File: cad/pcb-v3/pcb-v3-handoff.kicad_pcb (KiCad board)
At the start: 4 copper layers, 19.3 x 19.3 mm, 46 parts

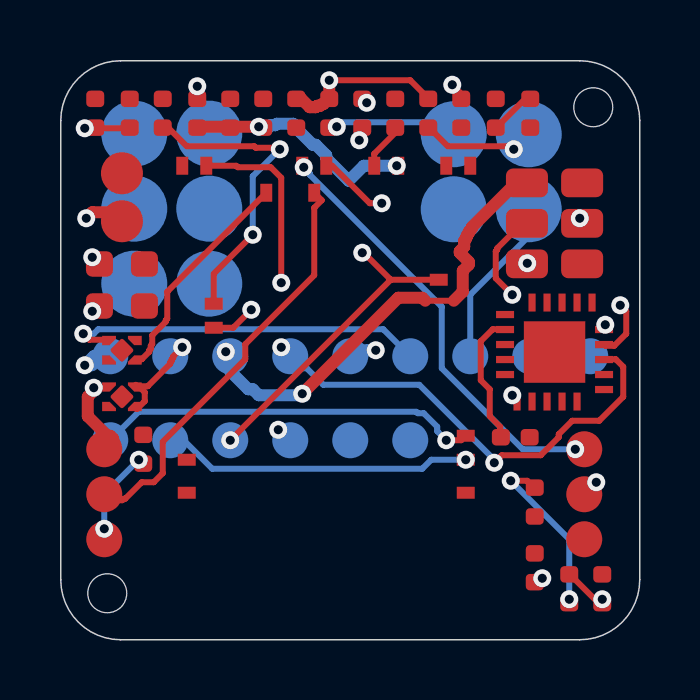
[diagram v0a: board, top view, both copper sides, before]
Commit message: pcb-v3: per-net plane-clean routing -> 12 opens with intact plane, 0 DRC, min track 0.200. Left column proven over-packed (0.225mm max gap vs 0.60 needed); BT1 is the cap. Board is over-subscribed in three places.
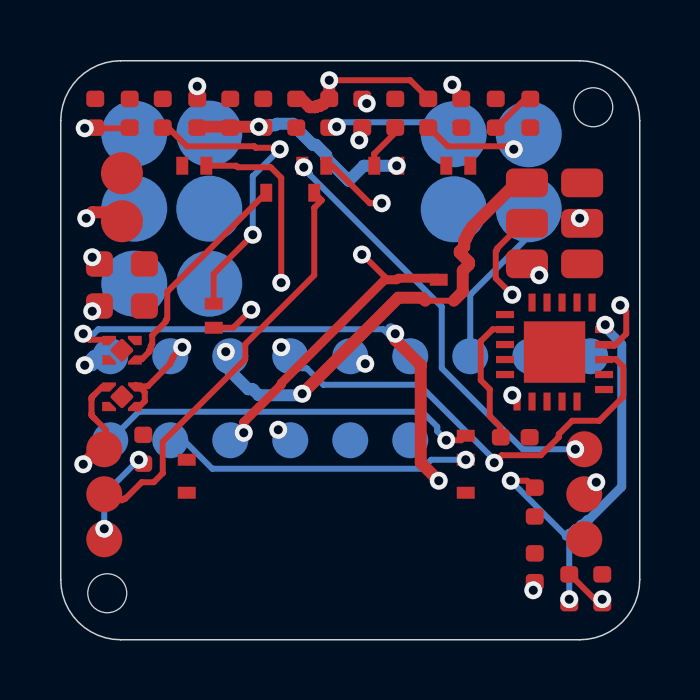
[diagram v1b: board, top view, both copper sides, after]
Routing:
- net SENSOR_MCU_3V3: track 15.5 -> 32.6 mm, vias 3 -> 5
- net OK_HYST: track 5.77 -> 13.8 mm
- net SENSOR_3V3: track 30.7 -> 34.0 mm
- net VBAT_OK: track 28.0 -> 30.2 mm

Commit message: pcb-v3: C1/C2 0603->0402 into the packer, C5/C7 0805->0603, left column down to U3+U4. 22 parts in 22 slots. Route: 12 -> 7 opens, plane untouched naturally, min track 0.200, vias 0.6/0.3.
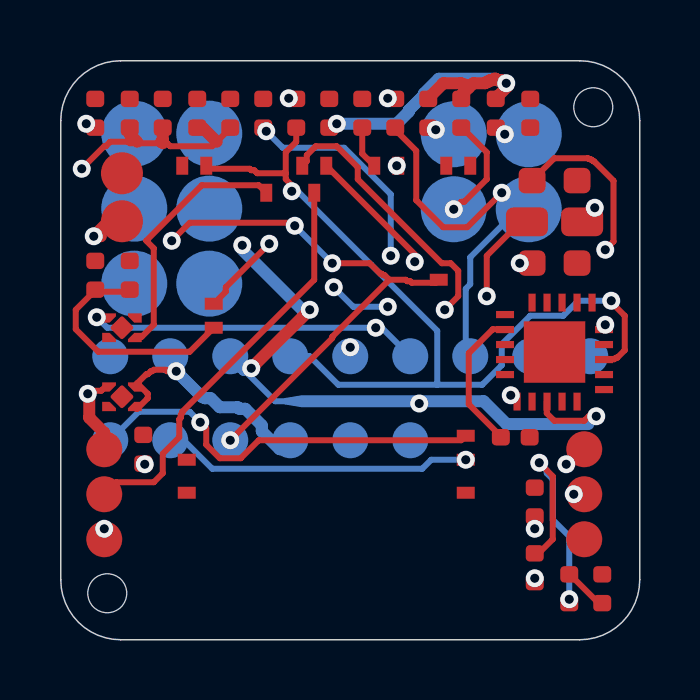
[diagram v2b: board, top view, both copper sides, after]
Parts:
- moved C6 17.6 mm to (-2.90, -7.90)
- moved ROV2 13.0 mm to (6.15, 5.06)
- moved C1 9.44 mm to (-0.70, -7.90), turned to 90 degrees
- moved C2 5.62 mm to (-5.10, -7.90), turned to 90 degrees
- moved C12 5.52 mm to (-8.50, -2.50)
- moved R5 5.52 mm to (-7.35, -2.50)
- moved R3 5.50 mm to (3.70, -7.90)
- moved R1 3.30 mm to (2.60, -7.90)
- moved C10 2.25 mm to (-6.25, -7.90)
- moved C13 2.25 mm to (-8.50, -7.90)
- moved R4 2.25 mm to (-7.35, -7.90)
- moved R2 2.25 mm to (4.85, -7.90)
- moved R6 2.20 mm to (1.50, -7.90)
- moved R7 2.20 mm to (-1.80, -7.90)
- moved ROK3 2.19 mm to (6.15, 7.25)
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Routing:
- net VBAT: track 23.5 -> 53.0 mm, vias 3 -> 9
- net VSTOR: track 16.1 -> 39.1 mm, vias 5 -> 3
- net OK_PROG: track 13.6 -> 1.55 mm, vias 2 -> 0
- net RESET: track 16.2 -> 24.4 mm, vias 3 -> 5
- net SENSOR_MCU_3V3: track 32.6 -> 24.6 mm, vias 5 -> 4
- net VBAT_SENSE: track 15.9 -> 8.04 mm, vias 3 -> 0
- net BL_RETURN: track 5.71 -> 13.2 mm, vias 0 -> 1
- net VIN_DC: track 9.81 -> 17.1 mm, vias 4 -> 3
- net SENSOR_3V3: track 34.0 -> 28.4 mm, vias 4 -> 5
- net SENSOR_TX: track 14.5 -> 18.2 mm
- net HARV_3: track 0.00 -> 3.60 mm, vias 0 -> 1
- net HARV_1: track 4.40 -> 0.86 mm
- net HARV_2: track 3.85 -> 1.18 mm
- net VRDIV: track 0.00 -> 2.36 mm, vias 0 -> 2
- net BL_FLAG: track 17.5 -> 19.8 mm
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
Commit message: pcb-v3: silkscreen (F.Fab designators, pin-1 dots, back identity block). Fix two checker bugs: KiCad Y-down rotation sign (79 phantom shorts) and rule-area layer scoping (47 phantom boxed pads). All gates clean; 7 opens, plane intact.
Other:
- board text added: "BT1 +"
- board text added: "Daniel Rivera"
- board text added: "J2"
- board text added: "TouchID v3 2026"
- board text added: "U1"
- board text added: "U2"
- board text added: "driver0"

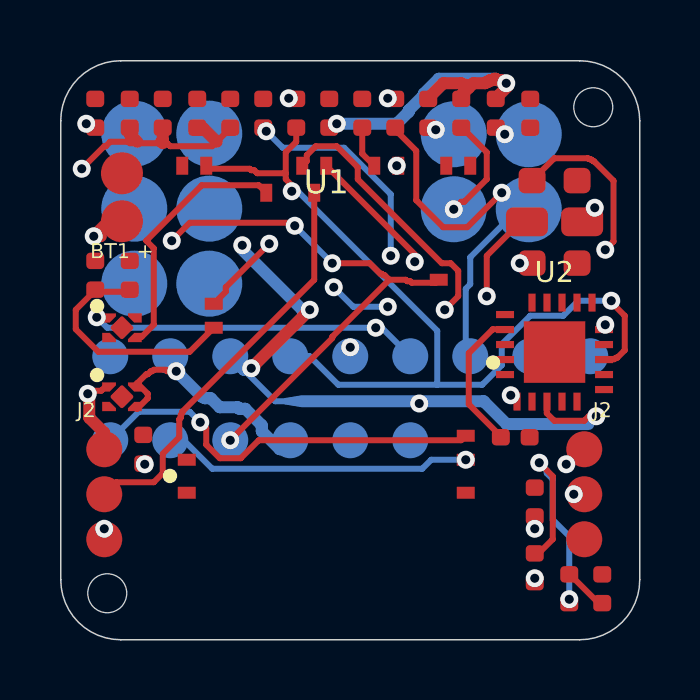
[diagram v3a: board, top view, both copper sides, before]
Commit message: pcb-v3: emit Raytac's second (top-layer-only) antenna keep-out. It was captured in mdbt50q_footprint.py as KEEPOUT_TOP and never written to the board.
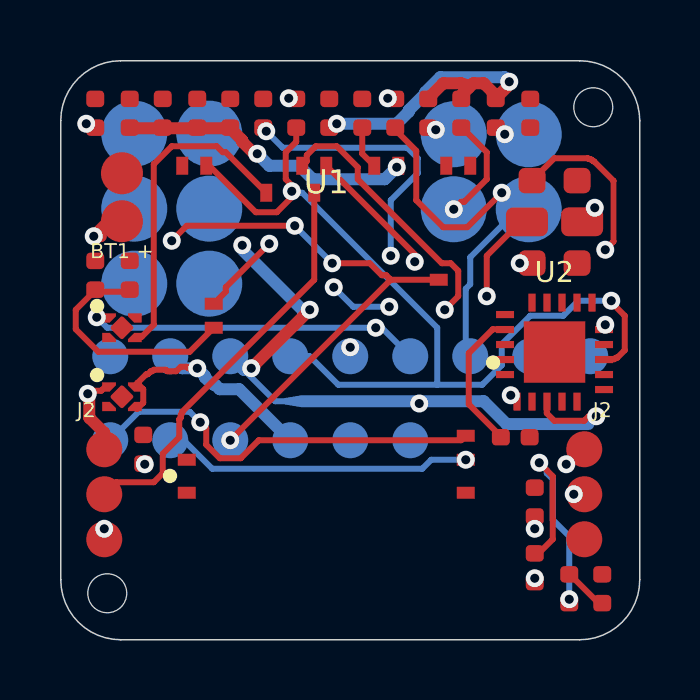
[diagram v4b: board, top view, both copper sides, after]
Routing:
- net VSTOR: track 39.1 -> 28.1 mm
- net SENSOR_SW_EN: track 8.44 -> 10.7 mm
- net SENSOR_3V3: track 28.4 -> 30.4 mm
- net VBAT_OK: track 28.9 -> 30.1 mm

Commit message: pcb-v3: re-source footprints from JLCPCB (L1 0.96->2.20mm was badly wrong), keep TI's land for U2 where JLC's is wider and riskier. Remove name from silk, add connector pinout labels + pin-1 dots.
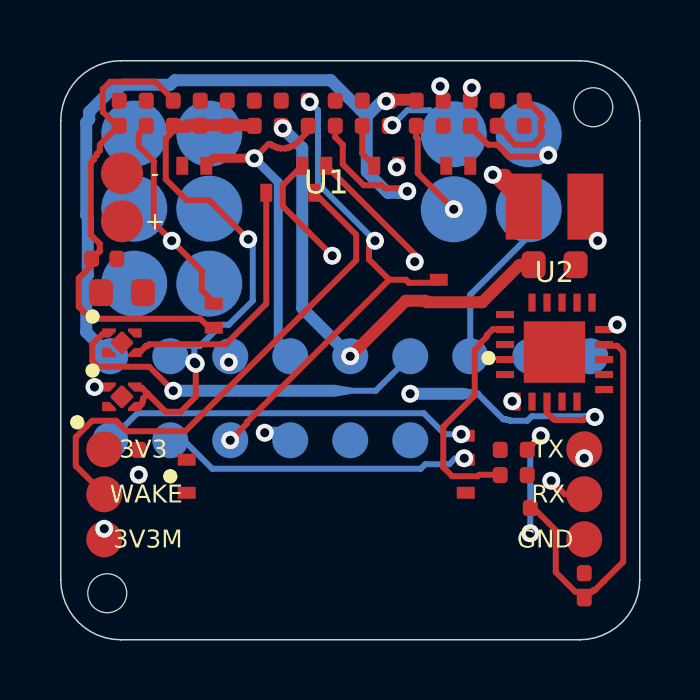
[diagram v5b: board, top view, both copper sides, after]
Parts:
- moved C5 14.9 mm to (-7.61, -1.92)
- moved ROV2 13.0 mm to (5.80, -7.90)
- moved R5 5.41 mm to (-7.70, -7.90)
- moved ROK3 3.52 mm to (5.90, 3.74)
- moved ROK2 2.62 mm to (6.00, 5.68)
- moved C2 1.90 mm to (-3.20, -7.90)
- moved C13 1.70 mm to (-6.80, -7.90)
- moved R6 1.60 mm to (3.10, -7.90)
- moved R3 1.50 mm to (2.20, -7.90)
- moved R4 1.45 mm to (-5.90, -7.90)
- moved R1 1.30 mm to (1.30, -7.90)
- moved C10 1.25 mm to (-5.00, -7.90)
- moved ROV1 1.10 mm to (4.90, -7.90)
- moved C4 0.98 mm to (5.00, 3.74), turned to 90 degrees
- moved R2 0.85 mm to (4.00, -7.90)
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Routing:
- net VBAT: track 53.0 -> 15.7 mm, vias 9 -> 3
- net VIN_DC: track 17.0 -> 36.5 mm, vias 3 -> 4
- net VBAT_OK: track 30.1 -> 11.3 mm, vias 2 -> 1
- net OK_PROG: track 1.55 -> 13.2 mm
- net RESET: track 24.4 -> 16.2 mm, vias 5 -> 3
- net VBAT_SENSE: track 8.04 -> 15.9 mm
- net BL_RETURN: track 13.2 -> 5.71 mm, vias 1 -> 0
- net SENSOR_MCU_3V3: track 24.6 -> 18.5 mm, vias 4 -> 3
- net OK_HYST: track 14.1 -> 9.53 mm
- net SENSOR_3V3: track 30.4 -> 26.5 mm, vias 5 -> 3
- net SENSOR_WAKEUP: track 13.7 -> 17.2 mm
- net VBAT_OV_SET: track 0.00 -> 3.46 mm
- net VREF_SAMP: track 4.77 -> 7.73 mm
- net HARV_2: track 1.18 -> 3.97 mm
- net VRDIV: track 2.36 -> 0.00 mm, vias 2 -> 0
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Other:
- board text added: "+"
- board text added: "-"
- board text added: "3V3"
- board text added: "3V3M"
- board text added: "CLK"
- board text added: "DIO"
- board text added: "GND"
- board text added: "RST"
- board text added: "RX"
- board text added: "TX"
- board text added: "VDD"
- board text added: "WAKE"
- board text removed: "BT1 +"
- board text removed: "Daniel Rivera"
- board text removed: "J2"

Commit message: 3D: generate STEP bodies at verified dimensions and attach to all 29 footprints so KiCad Alt+3 shows real geometry. Re-route: 8 opens, plane intact.
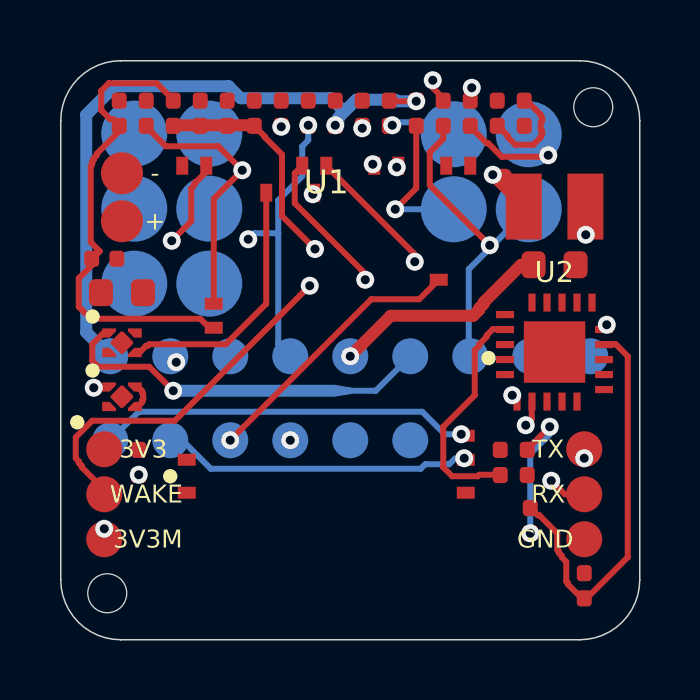
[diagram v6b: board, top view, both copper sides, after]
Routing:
- net VBAT: track 15.7 -> 0.00 mm, vias 3 -> 0
- net VSTOR: track 30.4 -> 39.1 mm
- net RESET: track 16.2 -> 9.17 mm, vias 3 -> 1
- net VIN_DC: track 36.5 -> 29.9 mm
- net BL_RETURN: track 5.71 -> 10.8 mm, vias 0 -> 1
- net VBAT_OK: track 11.3 -> 15.2 mm, vias 1 -> 3
- net SENSOR_3V3: track 26.5 -> 24.3 mm
- net HARV_3: track 3.32 -> 5.04 mm
- net SENSOR_WAKEUP: track 17.2 -> 15.6 mm, vias 0 -> 2
- net BL_FLAG: track 18.9 -> 17.7 mm
- net SENSOR_TX: track 17.6 -> 18.5 mm
- net NRF_VDD: track 1.49 -> 1.34 mm, vias 0 -> 2

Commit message: preflight.py: single pre-order gate (15 checks). Found 3 checker bugs of my own (pad-net regex scope, layer-blind keep-outs, silk-vs-wrong-side pads) and 2 real issues (silk over pads, LX has no 0.40 trunk). 13/15 pass.
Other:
- board text removed: "U1"
- board text removed: "U2"
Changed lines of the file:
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@@
-	)
-	(gr_text
-		"U1"
-		(at -0.8 -5.6)
-		(layer "F.SilkS")
-		(effects (font (size 0.8 0.8) (thickness 0.1)))
-	)
-	(gr_text
-		"U2"
-		(at 6.8 -2.6)
-		(layer "F.SilkS")
-		(effects (font (size 0.7 0.7) (thickness 0.1)))
 	)
 	(gr_text
 		"3V3"
-		(at -6.9 3.3)
-		(layer "F.SilkS")
-		(effects (font (size 0.6 0.6) (thickness 0.1)))
-	)
-	(gr_text
-		"3V3"
-		(at -6.9 3.3)
+		(at -6.888 3.3)
 		(layer "F.Fab")
 		(effects (font (size 0.4 0.4) (thickness 0.06)))
@@
 	(gr_text
 		"WAKE"
-		(at -6.8 4.8)
-		(layer "F.SilkS")
-		(effects (font (size 0.6 0.6) (thickness 0.1)))
-	)
-	(gr_text
-		"WAKE"
-		(at -6.8 4.8)
+		(at -6.7 4.8)
 		(layer "F.Fab")
 		(effects (font (size 0.4 0.4) (thickness 0.06)))
@@
 	(gr_text
 		"3V3M"
-		(at -6.75 6.3)
-		(layer "F.SilkS")
-		(effects (font (size 0.6 0.6) (thickness 0.1)))
-	)
-	(gr_text
-		"3V3M"
-		(at -6.75 6.3)
+		(at -6.7 6.3)
 		(layer "F.Fab")
 		(effects (font (size 0.4 0.4) (thickness 0.06)))
@@
 	(gr_text
 		"TX"
-		(at 6.6 3.3)
-		(layer "F.SilkS")
-		(effects (font (size 0.6 0.6) (thickness 0.1)))
-	)
-	(gr_text
-		"TX"
-		(at 6.6 3.3)
+		(at 6.675 3.3)
 		(layer "F.Fab")
 		(effects (font (size 0.4 0.4) (thickness 0.06)))
@@
 	(gr_text
 		"RX"
-		(at 6.6 4.8)
-		(layer "F.SilkS")
-		(effects (font (size 0.6 0.6) (thickness 0.1)))
-	)
-	(gr_text
-		"RX"
-		(at 6.6 4.8)
+		(at 6.675 4.8)
 		(layer "F.Fab")
 		(effects (font (size 0.4 0.4) (thickness 0.06)))
@@
 	(gr_text
 		"GND"
-		(at 6.5 6.3)
-		(layer "F.SilkS")
-		(effects (font (size 0.6 0.6) (thickness 0.1)))
-	)
-	(gr_text
-		"GND"
-		(at 6.5 6.3)
+		(at 6.488 6.3)
 		(layer "F.Fab")
 		(effects (font (size 0.4 0.4) (thickness 0.06)))
@@
 	(gr_text
 		"DIO"
-		(at -8.0 1.9)
-		(layer "B.SilkS")
-		(effects (font (size 0.6 0.6) (thickness 0.1)) (justify mirror))
-	)
-	(gr_text
-		"DIO"
-		(at -8.0 1.9)
+		(at -8.0 2.0)
 		(layer "F.Fab")
 		(effects (font (size 0.4 0.4) (thickness 0.06)))
@@
 	(gr_text
 		"CLK"
-		(at -6.0 1.9)
-		(layer "B.SilkS")
-		(effects (font (size 0.6 0.6) (thickness 0.1)) (justify mirror))
-	)
-	(gr_text
-		"CLK"
-		(at -6.0 1.9)
+		(at -6.0 2.0)
 		(layer "F.Fab")
 		(effects (font (size 0.4 0.4) (thickness 0.06)))
@@
 	(gr_text
 		"RST"
-		(at -4.0 1.9)
-		(layer "B.SilkS")
-		(effects (font (size 0.6 0.6) (thickness 0.1)) (justify mirror))
-	)
-	(gr_text
-		"RST"
-		(at -4.0 1.9)
+		(at -4.0 2.0)
 		(layer "F.Fab")
 		(effects (font (size 0.4 0.4) (thickness 0.06)))
@@
 	(gr_text
 		"VDD"
-		(at -2.0 1.9)
-		(layer "B.SilkS")
-		(effects (font (size 0.6 0.6) (thickness 0.1)) (justify mirror))
-	)
-	(gr_text
-		"VDD"
-		(at -2.0 1.9)
+		(at -2.0 2.0)
 		(layer "F.Fab")
 		(effects (font (size 0.4 0.4) (thickness 0.06)))
@@
 	(gr_text
 		"GND"
-		(at 0.0 1.9)
-		(layer "B.SilkS")
-		(effects (font (size 0.6 0.6) (thickness 0.1)) (justify mirror))
-	)
-	(gr_text
-		"GND"
-		(at 0.0 1.9)
+		(at 0.0 2.0)
 		(layer "F.Fab")
 		(effects (font (size 0.4 0.4) (thickness 0.06)))
@@
 	(gr_text
 		"+"
-		(at -6.51 -4.3)
+		(at -6.572 -4.3)
 		(layer "F.SilkS")
-		(effects (font (size 0.6 0.6) (thickness 0.1)))
+		(effects (font (size 0.5 0.5) (thickness 0.1)))
 	)
 	(gr_text
 		"+"
-		(at -6.51 -4.3)
+		(at -6.572 -4.3)
 		(layer "F.Fab")
 		(effects (font (size 0.4 0.4) (thickness 0.06)))
@@
 	(gr_text
 		"-"
-		(at -6.51 -5.9)
+		(at -6.572 -5.9)
 		(layer "F.SilkS")
-		(effects (font (size 0.6 0.6) (thickness 0.1)))
+		(effects (font (size 0.5 0.5) (thickness 0.1)))
 	)
 	(gr_text
 		"-"
-		(at -6.51 -5.9)
+		(at -6.572 -5.9)
 		(layer "F.Fab")
 		(effects (font (size 0.4 0.4) (thickness 0.06)))

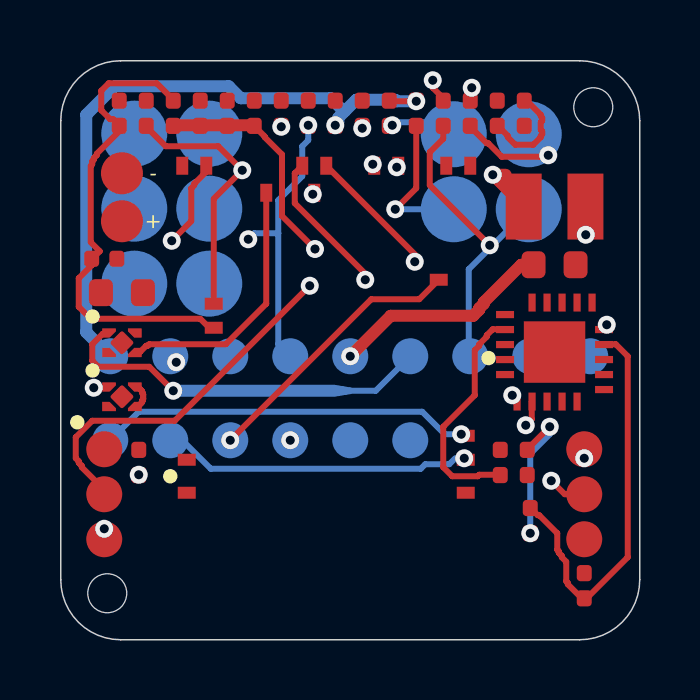
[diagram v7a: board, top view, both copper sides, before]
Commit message: U2 land was 0.25mm off its own centreline (even-count offset formula for an odd pad row). LX wrapped 11mm around the chip; L1 moved above U2 and flipped -> 1.91mm. Opens 8->7.
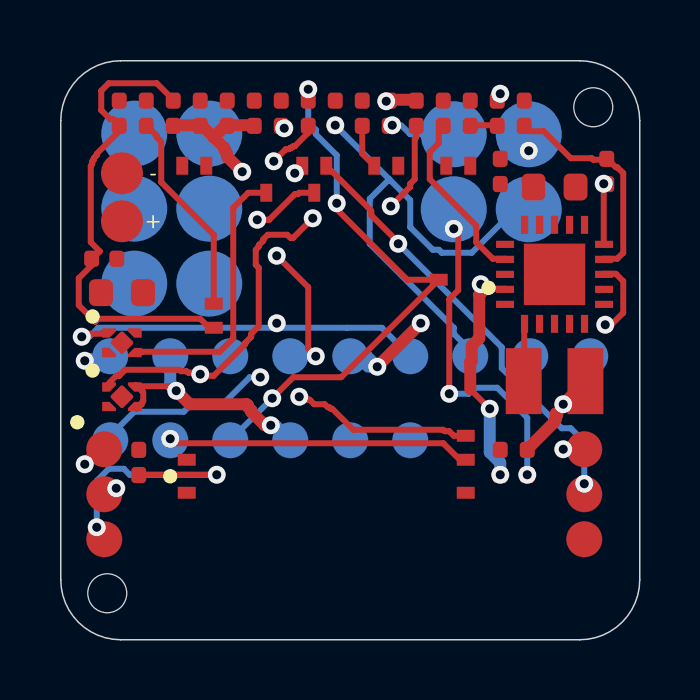
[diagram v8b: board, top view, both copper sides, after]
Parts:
- moved ROK1 15.9 mm to (5.80, -7.90)
- moved C1 12.9 mm to (5.00, 3.74)
- moved R3 12.2 mm to (5.90, 3.74)
- moved ROK2 11.9 mm to (8.55, -5.96)
- moved C4 11.8 mm to (3.10, -7.90)
- moved ROK3 11.7 mm to (4.90, -7.90)
- moved L1 5.82 mm to (6.81, 1.03), turned to 180 degrees
- moved R6 3.60 mm to (-0.50, -7.90)
- moved C7 2.59 mm to (6.81, -5.44)
- moved U2 2.59 mm to (6.81, -2.53)
- moved ROV1 1.94 mm to (5.00, -5.96)
- moved R2 1.80 mm to (2.20, -7.90)
- moved ROV2 1.80 mm to (4.00, -7.90)
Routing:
- net VSTOR: track 39.1 -> 21.1 mm, vias 5 -> 3
- net BL_FLAG: track 17.7 -> 6.90 mm, vias 2 -> 0
- net HARV_2: track 3.97 -> 14.3 mm, vias 1 -> 2
- net VBAT_OK: track 15.2 -> 25.1 mm, vias 3 -> 4
- net RESET: track 9.17 -> 18.3 mm, vias 1 -> 3
- net VIN_DC: track 29.9 -> 38.9 mm, vias 4 -> 6
- net SENSOR_MCU_3V3: track 18.5 -> 27.1 mm, vias 3 -> 4
- net SENSOR_3V3: track 24.3 -> 30.9 mm, vias 3 -> 6
- net HARV_3: track 5.04 -> 11.3 mm, vias 1 -> 3
- net BL_RETURN: track 10.8 -> 16.9 mm
- net OK_PROG: track 13.5 -> 7.43 mm
- net LX: track 7.58 -> 2.00 mm, vias 2 -> 0
- net VBAT_OV_SET: track 3.46 -> 0.00 mm
- net OK_HYST: track 9.12 -> 7.01 mm, vias 3 -> 2
- net VREF_SAMP: track 7.73 -> 5.83 mm
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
